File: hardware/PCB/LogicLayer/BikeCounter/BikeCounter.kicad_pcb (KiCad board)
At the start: 2 copper layers, 81.5 x 36.8 mm, 18 parts, among them J1 PIR sensor connector (TWIG-4P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, J2 Conn_01x04_Female, J3 Vbat, SW1 SW_DIP_x03, U1 DS3231M

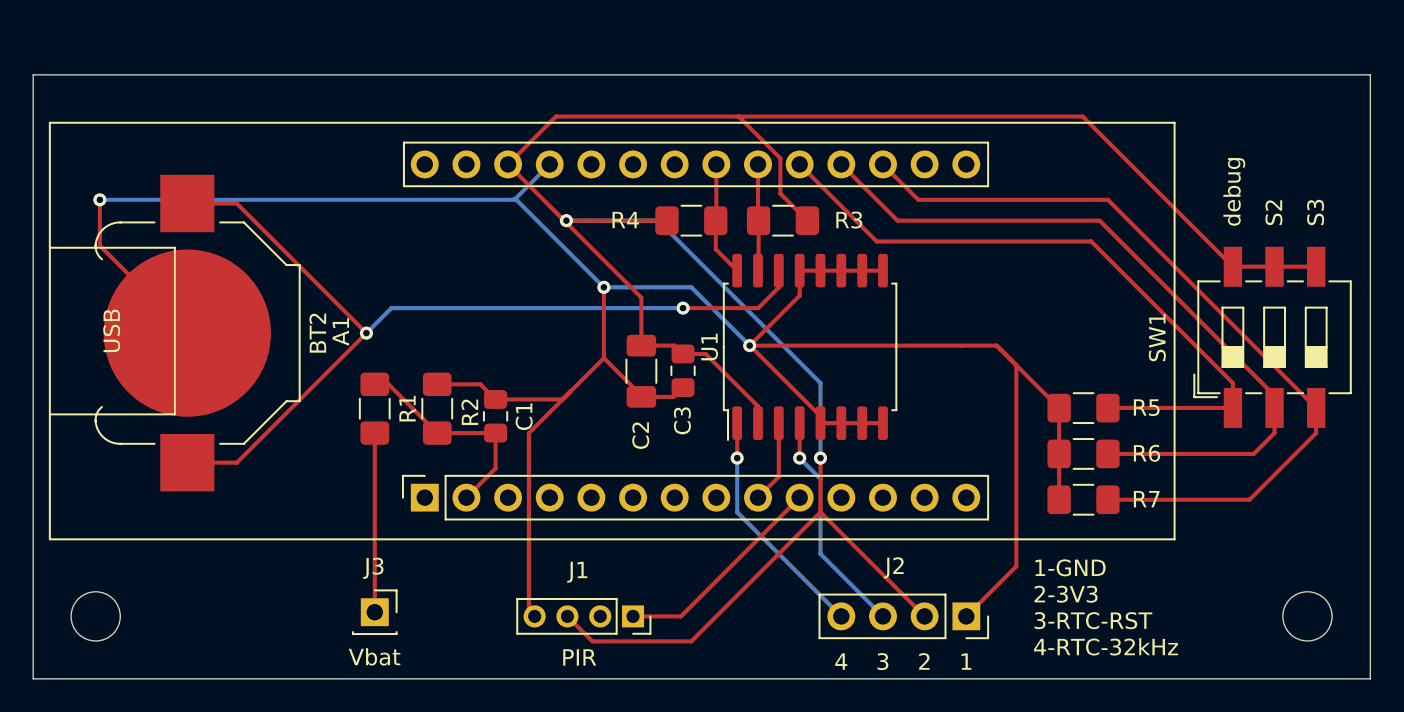
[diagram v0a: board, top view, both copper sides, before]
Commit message: Humidity sensor to pcb added
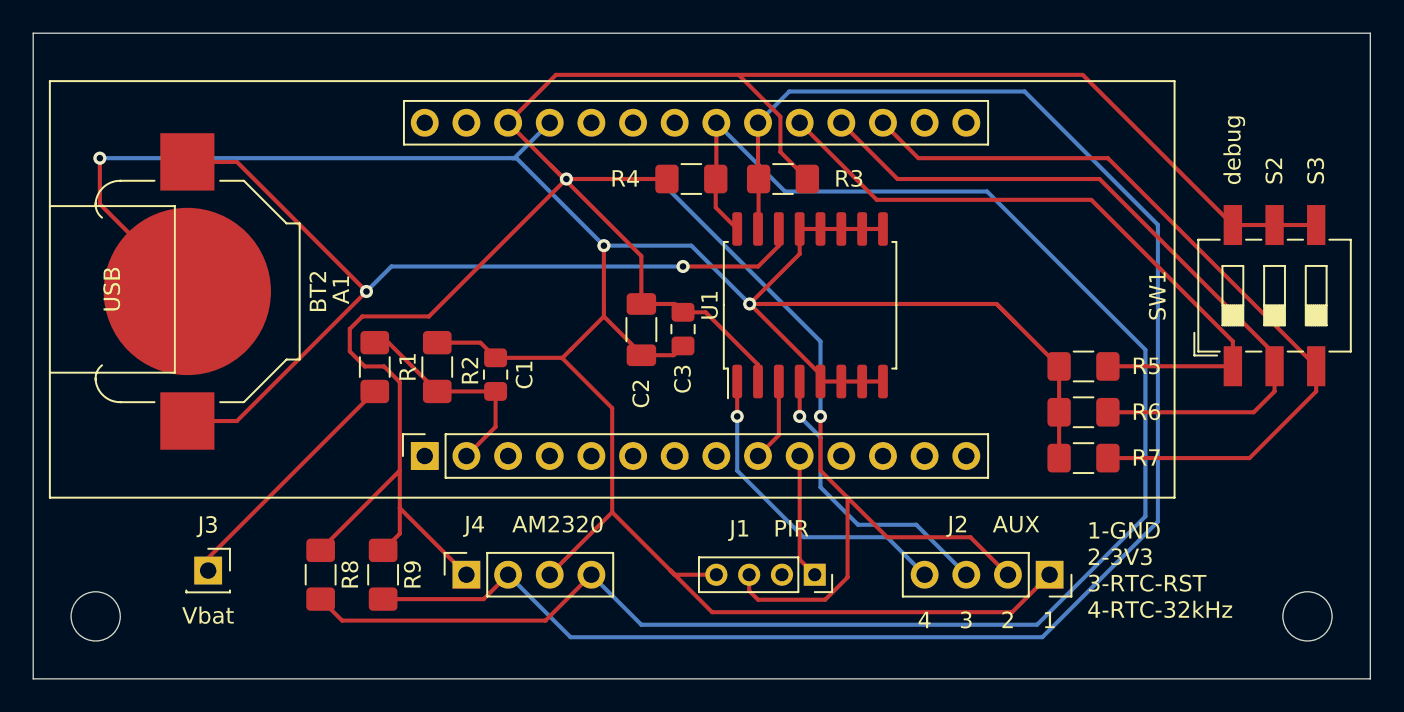
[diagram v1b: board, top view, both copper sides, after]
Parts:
- added J4: AM2320, Connector_PinSocket_2.54mm:PinSocket_1x04_P2.54mm_Vertical, F.Cu at (160.5, 81.3)
- added R8: 10k, Resistor_SMD:R_1206_3216Metric_Pad1.42x1.75mm_HandSolder, F.Cu at (151.6, 81.3)
- added R9: 10k, Resistor_SMD:R_1206_3216Metric_Pad1.42x1.75mm_HandSolder, F.Cu at (155.4, 81.3)
- J2: value Conn_01x04_Female -> AUX
- moved J1 11.4 mm to (181.8, 81.3)
- moved J3 10.5 mm to (144.8, 81.0)
- moved J2 5.68 mm to (196.1, 81.3)
- moved A1 2.54 mm to (158.0, 74.0)
- moved BT2 2.54 mm to (143.5, 64.0)
- moved C1 2.54 mm to (162.3, 69.1)
- moved C2 2.54 mm to (171.2, 66.3)
- moved C3 2.54 mm to (173.7, 66.3)
- moved R5 2.54 mm to (198.2, 68.6)
- moved R6 2.54 mm to (198.2, 71.4)
- moved SW1 2.54 mm to (209.8, 64.3)
- moved U1 2.54 mm to (181.5, 64.8)
- moved R3 2.54 mm to (179.8, 57.1)
- moved R4 2.54 mm to (174.2, 57.1)
- moved R1 2.54 mm to (154.9, 68.6)
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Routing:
- net SDA: track 6.51 -> 105.5 mm
- net SCL: track 7.03 -> 105.1 mm
- net +3V3: track 149.7 -> 193.5 mm
- net GND: track 159.3 -> 176.9 mm
- net PIR_signal: track 13.2 -> 7.62 mm
- net RTC_32KHZ: track 14.4 -> 19.5 mm
- net Net-(J3-Pad1): track 10.9 -> 15.1 mm
- net RTC_RST: track 13.9 -> 18.1 mm
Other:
- board size 81.5 x 36.8 mm -> 81.5 x 39.4 mm
- board text added: "BikeCounter logic layer github.com/guidosch/lora PCB v0.1"
- board text removed: "BikeCounter github.com/xxx PCB v0.1"

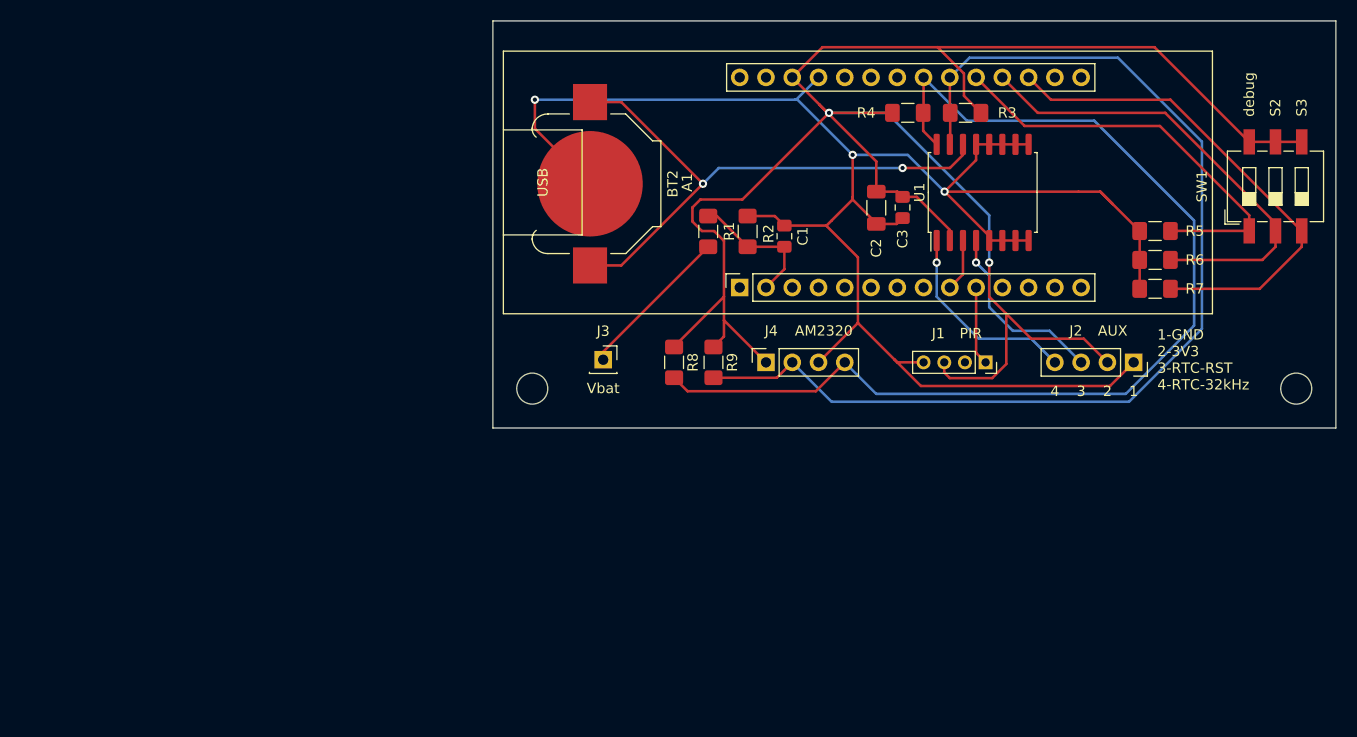
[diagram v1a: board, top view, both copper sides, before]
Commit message: Final casing selected and PCB rearranged to fit into the casing
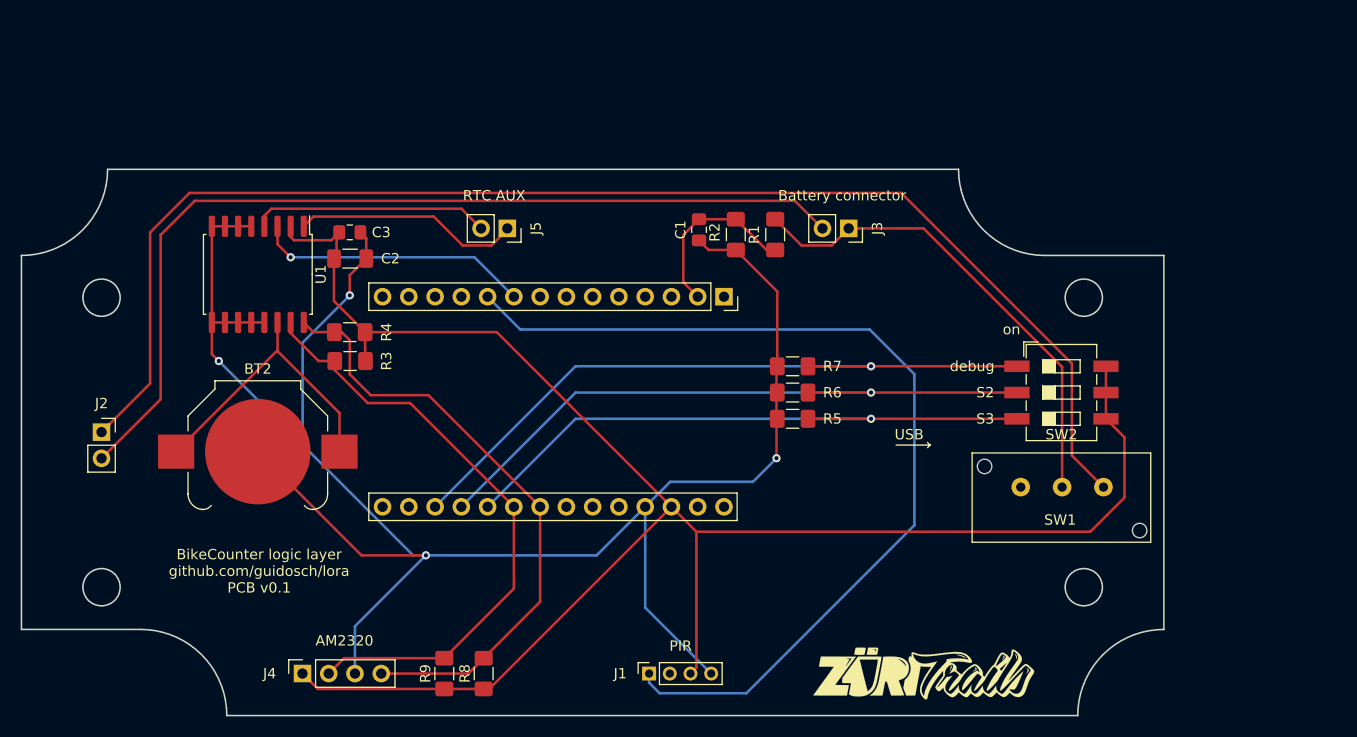
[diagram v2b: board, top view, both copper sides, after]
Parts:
- added G***: LOGO, ZueriTrailsLogo:ZueriTrailsLogo_small, F.Cu at (175.8, 111.4)
- added J5: RTC AUX, Connector_PinSocket_2.54mm:PinSocket_1x02_P2.54mm_Vertical, F.Cu at (135.5, 68.3)
- added SW1: SW_SPST, General_TM:Switch_MHS12204, F.Cu at (193.2, 93.3)
- J2: value AUX -> Power layer connector; footprint Connector_PinSocket_2.54mm:PinSocket_1x04_P2.54mm_Vertical -> Connector_PinSocket_2.54mm:PinSocket_1x02_P2.54mm_Vertical
- J3: value Vbat -> Battery connector; footprint Connector_PinSocket_2.54mm:PinSocket_1x01_P2.54mm_Vertical -> Connector_PinSocket_2.54mm:PinSocket_1x02_P2.54mm_Vertical
- moved J2 100.1 mm to (96.3, 88.0), turned to 0 degrees
- moved U1 70.6 mm to (111.4, 72.8), turned to 270 degrees
- moved R3 64.2 mm to (120.3, 81.2)
- moved R4 58.0 mm to (120.3, 78.4), turned to 180 degrees
- moved J4 54.0 mm to (115.7, 111.4)
- moved C3 53.5 mm to (120.3, 68.7), turned to 0 degrees
- moved C2 51.1 mm to (120.3, 71.2), turned to 0 degrees
- moved J1 44.3 mm to (149.2, 111.4), turned to 90 degrees
- moved BT2 41.3 mm to (111.4, 89.9), turned to 0 degrees
- moved R9 39.8 mm to (129.4, 111.4), turned to 90 degrees
- moved R5 39.5 mm to (163.1, 86.7)
- moved R6 37.3 mm to (163.1, 84.2)
- moved G*** 36.3 mm to (144.4, 84.8)
- moved R7 35.8 mm to (163.1, 81.7)
- moved R8 35.3 mm to (133.2, 111.4), turned to 90 degrees
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- renumbered SW1 to SW2
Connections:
- J2 pad 1: GND -> Net-(J2-Pad1)
- J2 pad 2: +3V3 -> Net-(J2-Pad2)
- SW2 pad 1: Net-(A1-Pad19) -> Net-(A1-Pad17)
- SW2 pad 3: Net-(A1-Pad17) -> Net-(A1-Pad19)
- U1 pad 1: RTC_32KHZ -> RTC_32kHz
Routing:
- net Net-(J2-Pad1): track 0.00 -> 132.0 mm
- net Net-(J2-Pad2): track 0.00 -> 90.5 mm
- net PIR_signal: track 7.62 -> 92.7 mm
- net SDA: track 105.5 -> 59.3 mm
- net SCL: track 105.1 -> 59.6 mm
- net Net-(J3-Pad1): track 15.1 -> 46.7 mm
- net Net-(BT2-Pad1): track 55.7 -> 28.8 mm, vias 2 -> 0
- net RTC_32kHz: track 0.00 -> 22.0 mm
- net RTC_timer: track 5.07 -> 26.7 mm, vias 0 -> 1
- net Net-(A1-Pad19): track 41.1 -> 60.8 mm, vias 0 -> 1
- net +3V3: track 193.5 -> 173.9 mm, vias 2 -> 0
- net Net-(A1-Pad17): track 48.5 -> 68.0 mm, vias 0 -> 1
- net RTC_32KHZ: track 19.5 -> 0.00 mm, vias 1 -> 0
- net Net-(A1-Pad18): track 45.2 -> 64.4 mm, vias 0 -> 1
- net GND: track 176.9 -> 190.4 mm, vias 3 -> 4
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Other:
- board size 81.5 x 39.4 mm -> 110.5 x 52.8 mm
- board text added: "on"
- board text removed: "1"
- board text removed: "1-GND 2-3V3 3-RTC-RST 4-RTC-32kHz"
- board text removed: "2"
- board text removed: "3"
- board text removed: "4"

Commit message: PCB adjusted and BOM started
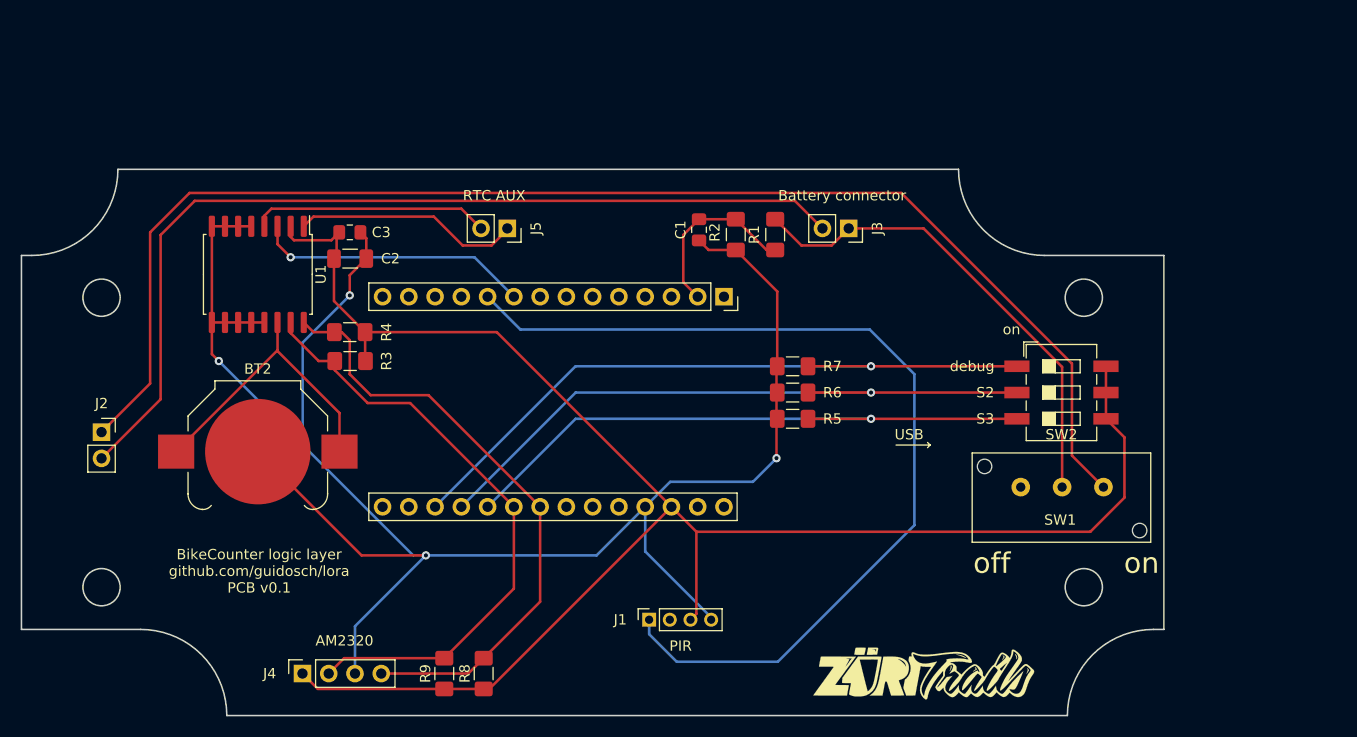
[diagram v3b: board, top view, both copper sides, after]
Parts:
- moved J1 5.21 mm to (149.2, 106.2)
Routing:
- net GND: track 190.4 -> 185.2 mm
- net +3V3: track 173.9 -> 168.7 mm
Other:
- outline, holes or cut-outs redrawn
- board text added: "off"

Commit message: BOM finished and Gerber files created
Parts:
- added REF**: MountingHole_3.5mm_Pad, MountingHole:MountingHole_3.5mm_Pad, F.Cu at (191.3, 75.0)
- added REF**: MountingHole_3.5mm_Pad, MountingHole:MountingHole_3.5mm_Pad, F.Cu at (191.3, 103.0)
- added REF**: MountingHole_3.5mm_Pad, MountingHole:MountingHole_3.5mm_Pad, F.Cu at (96.3, 103.0)
- added REF**: MountingHole_3.5mm_Pad, MountingHole:MountingHole_3.5mm_Pad, F.Cu at (96.3, 75.0)
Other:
- outline, holes or cut-outs redrawn

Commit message: pcb v0.2 started
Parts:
- removed BT2: Battery_Cell, Battery:BatteryHolder_Keystone_3000_1x12mm
- removed C2: 10uF, Capacitor_SMD:C_1206_3216Metric_Pad1.33x1.80mm_HandSolder
- removed C3: 0.1uF, Capacitor_SMD:C_0805_2012Metric_Pad1.15x1.40mm_HandSolder
- removed J5: RTC AUX, Connector_PinSocket_2.54mm:PinSocket_1x02_P2.54mm_Vertical
- removed R3, R4: 10k, Resistor_SMD:R_1206_3216Metric_Pad1.42x1.75mm_HandSolder
- removed U1: DS3231M, Package_SO:SOIC-16W_7.5x10.3mm_P1.27mm
- C1: footprint Capacitor_SMD:C_0805_2012Metric_Pad1.15x1.40mm_HandSolder -> Capacitor_SMD:C_0805_2012Metric_Pad1.18x1.45mm_HandSolder
- R1, R2, R5, R6, R7, R8, R9: footprint Resistor_SMD:R_1206_3216Metric_Pad1.42x1.75mm_HandSolder -> Resistor_SMD:R_1206_3216Metric_Pad1.30x1.75mm_HandSolder
- moved A1 5.97 mm to (150.5, 74.9)
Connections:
- A1 pad 1: Net-(A1-Pad1) -> unconnected-(A1-AREF-Pad1)
- A1 pad 11: Net-(A1-Pad11) -> PIR_power
- A1 pad 12: Net-(A1-Pad12) -> unconnected-(A1-D3-Pad12)
- A1 pad 13: Net-(A1-Pad13) -> unconnected-(A1-D4-Pad13)
- A1 pad 14: Net-(A1-Pad14) -> unconnected-(A1-D5-Pad14)
- A1 pad 15: Net-(A1-Pad15) -> unconnected-(A1-D6-Pad15)
- A1 pad 16: Net-(A1-Pad16) -> unconnected-(A1-D7-Pad16)
- A1 pad 22: Net-(A1-Pad22) -> unconnected-(A1-D13-Pad22)
- A1 pad 23: Net-(A1-Pad23) -> unconnected-(A1-D14-Pad23)
- A1 pad 24: Net-(A1-Pad24) -> unconnected-(A1-RESET-Pad24)
- A1 pad 27: Net-(A1-Pad27) -> unconnected-(A1-VIN-Pad27)
- A1 pad 28: Net-(A1-Pad28) -> unconnected-(A1-+5V-Pad28)
- A1 pad 3: Net-(A1-Pad3) -> unconnected-(A1-A1-Pad3)
- A1 pad 4: Net-(A1-Pad4) -> unconnected-(A1-A2-Pad4)
- A1 pad 5: Net-(A1-Pad5) -> unconnected-(A1-A3-Pad5)
- A1 pad 6: Net-(A1-Pad6) -> unconnected-(A1-A4-Pad6)
- A1 pad 7: Net-(A1-Pad7) -> unconnected-(A1-A5-Pad7)
- A1 pad 8: Net-(A1-Pad8) -> unconnected-(A1-A6-Pad8)
- A1 pad 9: RTC_timer -> unconnected-(A1-D0-Pad9)
- J1 pad 2: Net-(J1-Pad2) -> unconnected-(J1-Pin_2-Pad2)
- J1 pad 3: +3V3 -> PIR_power
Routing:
- net PIR_power: track 0.00 -> 91.7 mm
- net GND: track 185.2 -> 94.8 mm, vias 4 -> 197
- net +3V3: track 168.7 -> 107.2 mm
- net SCL: track 59.6 -> 25.4 mm
- net SDA: track 59.3 -> 27.3 mm
- net Net-(BT2-Pad1): track 28.8 -> 0.00 mm
- net RTC_timer: track 26.7 -> 0.00 mm, vias 1 -> 0
- net RTC_RST: track 23.0 -> 0.00 mm
- net RTC_32kHz: track 22.0 -> 0.00 mm
- net Net-(A1-D8): track 68.0 -> 75.8 mm
- net Net-(A1-D9): track 64.4 -> 71.5 mm
- net PIR_signal: track 92.6 -> 99.5 mm
- net Net-(A1-D10): track 60.8 -> 67.5 mm
- net Net-(A1-A0): track 17.3 -> 20.0 mm
- net Net-(J2-Pin_1): track 132.0 -> 133.0 mm
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- added copper zone on B.Cu, net GND
- added copper zone on F.Cu, net GND
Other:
- net class Default removed
- board text added: "BikeCounter logic layer (PCB v0.2) github.com/guidosch/bikecounter"
- board text removed: "BikeCounter logic layer github.com/guidosch/lora PCB v0.1"
